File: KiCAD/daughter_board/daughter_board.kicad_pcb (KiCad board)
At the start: 2 copper layers, 41 x 33 mm, 29 parts, among them IC1 QMC5883L, J1 JST, J2 S2B-PH-SM4-TB_LF__SN_2mm, U1 TPS61023DRLR, U2 SN74AHCT1G125DBVR, U3 XIAO-ESP32-C3-SMD, U4 MPU-6050

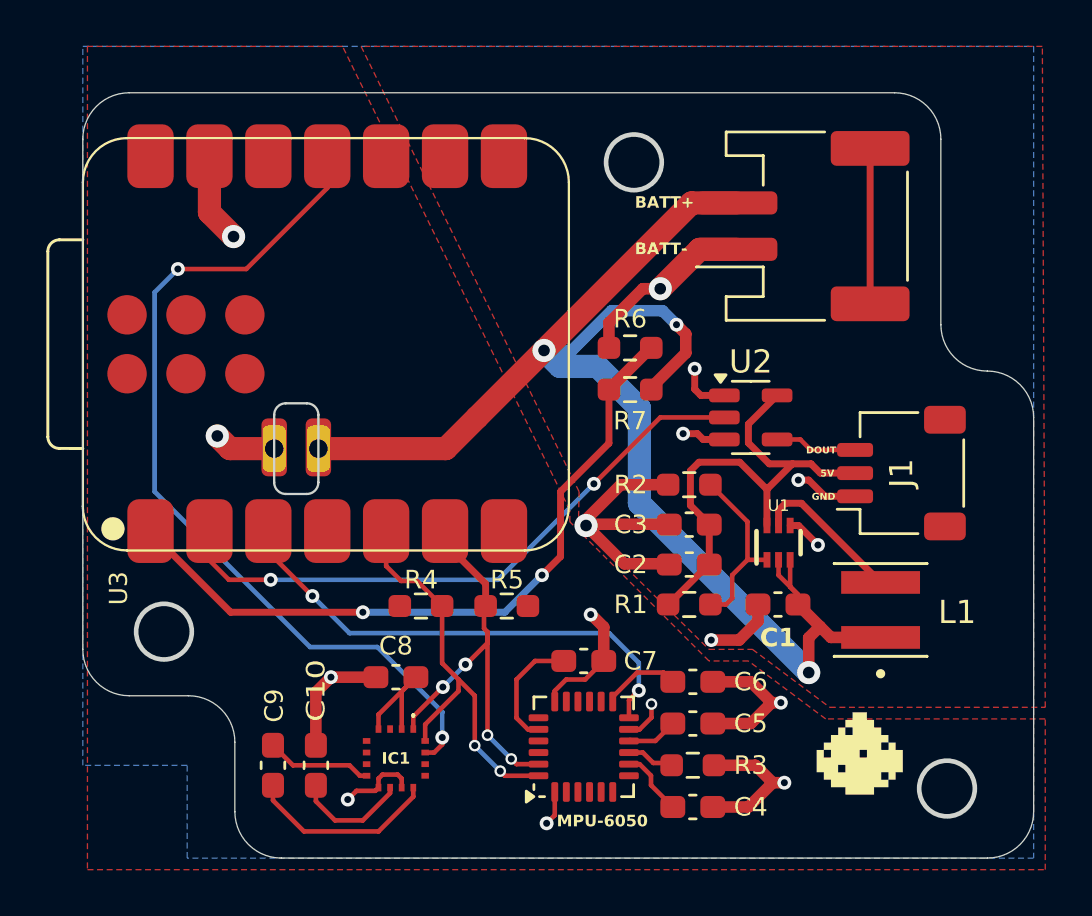
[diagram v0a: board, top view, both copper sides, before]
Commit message: in the pcb of daughter board, change the ground pour plane from top to bottom and power plane from bottom to top
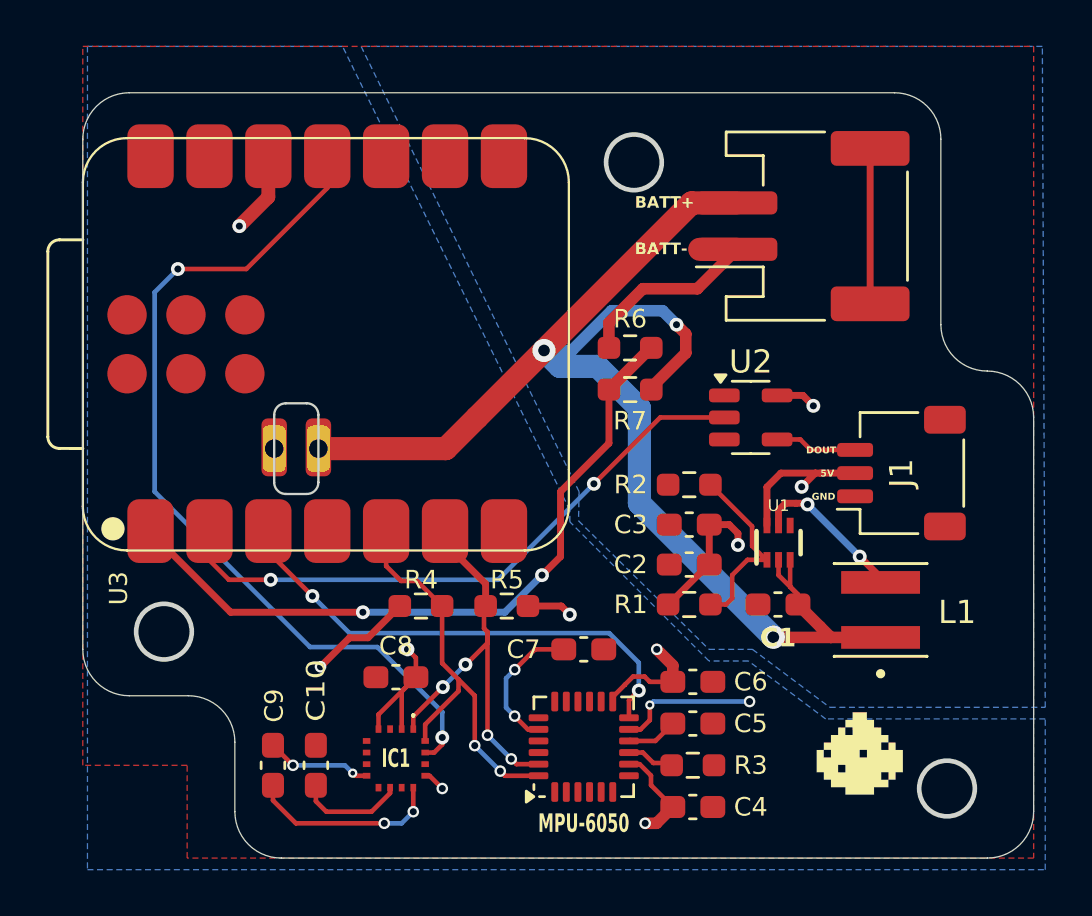
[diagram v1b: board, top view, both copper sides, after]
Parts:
- moved C7 0.50 mm to (104.6, 63.0)
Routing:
- net -BATT: track 68.1 -> 15.6 mm, vias 16 -> 2
- net /3V3: track 11.8 -> 27.3 mm, vias 0 -> 7
- net /5V: track 21.6 -> 14.8 mm, vias 0 -> 3
- net +BATT: track 62.5 -> 60.6 mm
- net Net-(U4-CPOUT): track 5.18 -> 6.05 mm, vias 0 -> 2
- net Net-(U1-SW): track 6.60 -> 6.72 mm, vias 0 -> 2
- net Net-(IC1-SETC): track 8.26 -> 8.35 mm, vias 0 -> 2
- net Net-(IC1-STEP): vias 0 -> 2
- added copper zone on F.Cu, net -BATT
- added copper zone on B.Cu, net /3V3
- added copper zone on B.Cu, net /5V
- removed copper zone on B.Cu, net -BATT
- removed copper zone on F.Cu, net /3V3
- removed copper zone on F.Cu, net /5V

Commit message: changed the min via hole so that min via hole=0.3mm
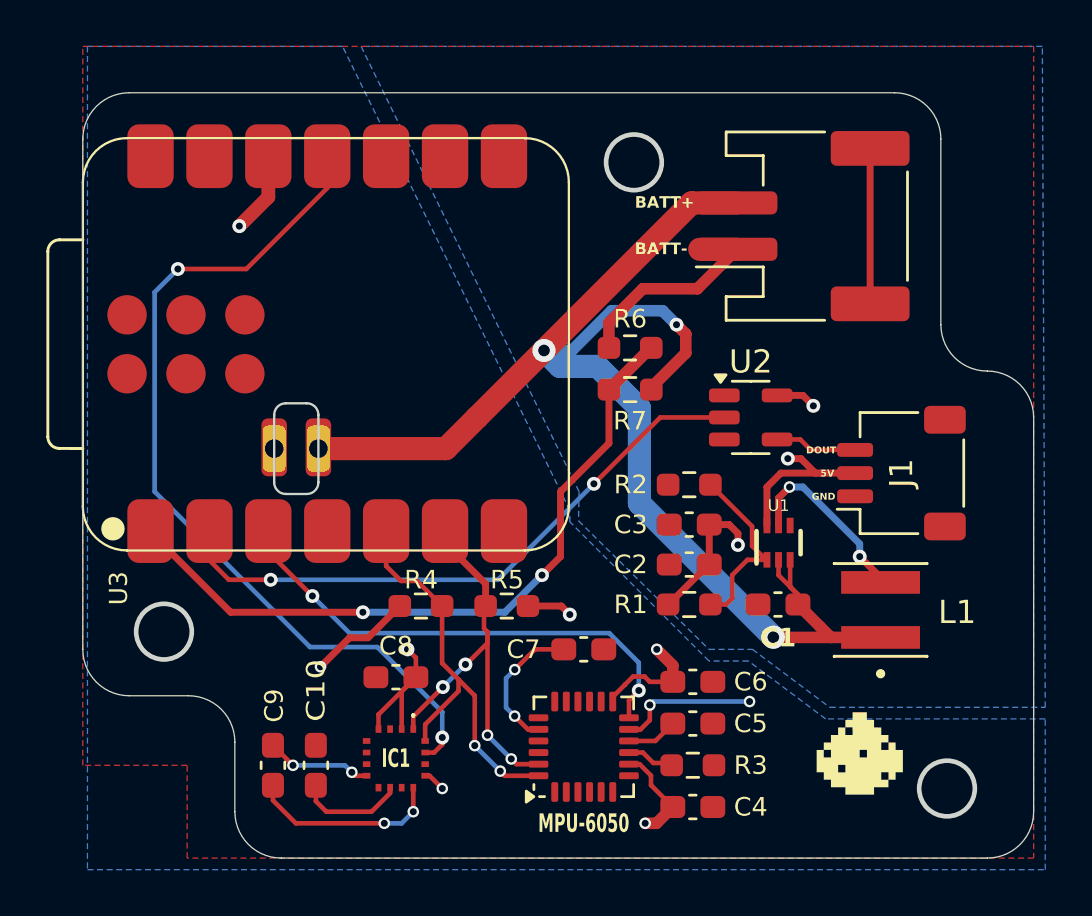
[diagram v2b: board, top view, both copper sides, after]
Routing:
- net Net-(U1-SW): track 6.72 -> 7.93 mm
- net /5V: track 14.8 -> 15.4 mm
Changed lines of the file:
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@@
 	(via
 		(at 107.45 65.4)
-		(size 0.4)
-		(drill 0.2)
+		(size 0.5)
+		(drill 0.3)
 		(layers "F.Cu" "B.Cu")
 		(net 2)
@@
 	)
 	(segment
-		(start 113.997017 55.991051)
-		(end 114.588068 55.4)
-		(width 0.3)
-		(layer "F.Cu")
-		(net 3)
-	)
-	(segment
 		(start 112.498998 57.659999)
 		(end 112.498997 56.001003)
@@
 	)
 	(segment
+		(start 113.4 54.775)
+		(end 113.963068 54.775)
+		(width 0.3)
+		(layer "F.Cu")
+		(net 3)
+	)
+	(segment
 		(start 112.498997 56.001003)
 		(end 113.1 55.4)
@@
 		(net 3)
 	)
+	(segment
+		(start 113.963068 54.775)
+		(end 114.588068 55.4)
+		(width 0.3)
+		(layer "F.Cu")
+		(net 3)
+	)
 	(via
 		(at 111.25 58.5)
@@
 	)
 	(via
-		(at 113.997017 55.991051)
+		(at 113.4 54.775)
 		(size 0.6)
 		(drill 0.3)
@@
 	(segment
 		(start 94.75 68.45)
-		(end 95.237 68.45)
+		(end 94.6 68.3)
 		(width 0.2)
 		(layer "F.Cu")
@@
 	)
 	(segment
-		(start 94.638928 68.338928)
+		(start 95.237 68.45)
 		(end 94.75 68.45)
 		(width 0.2)
@@
 	)
 	(via
-		(at 94.638928 68.338928)
-		(size 0.4)
-		(drill 0.2)
+		(at 94.6 68.3)
+		(size 0.5)
+		(drill 0.3)
 		(layers "F.Cu" "B.Cu")
 		(net 8)
@@
 	)
 	(segment
-		(start 94.638928 68.338928)
+		(start 94.6 68.3)
 		(end 94.3 68)
 		(width 0.2)
@@
 	)
 	(segment
-		(start 113.3 56.7)
-		(end 113.75 56.7)
-		(width 0.3)
-		(layer "F.Cu")
-		(net 20)
-	)
-	(segment
 		(start 117.4 59.9)
 		(end 117.4 60.115)
@@
 	)
 	(segment
-		(start 113.75 56.7)
-		(end 114.2 56.7)
-		(width 0.3)
-		(layer "F.Cu")
-		(net 20)
-	)
-	(segment
-		(start 114.2 56.7)
-		(end 114.25 56.75)
-		(width 0.3)
-		(layer "F.Cu")
-		(net 20)
-	)
-	(segment
 		(start 116.5 59)
 		(end 117.4 59.9)
@@
 	)
 	(segment
-		(start 112.999997 57.000003)
-		(end 113.3 56.7)
+		(start 113 56.475)
+		(end 113.475 56)
 		(width 0.3)
 		(layer "F.Cu")
@@
 	)
 	(segment
+		(start 113 57.659996)
+		(end 113 56.475)
+		(width 0.3)
+		(layer "F.Cu")
+		(net 20)
+	)
+	(segment
 		(start 112.999997 57.659999)
-		(end 112.999997 57.000003)
+		(end 113 57.659996)
 		(width 0.3)
 		(layer "F.Cu")
@@
 	)
 	(via
-		(at 114.25 56.75)
-		(size 0.6)
+		(at 113.475 56)
+		(size 0.5)
 		(drill 0.3)
 		(layers "F.Cu" "B.Cu")
@@
 	)
 	(segment
-		(start 114.25 56.75)
+		(start 116.5 58.45)
 		(end 116.5 59)
 		(width 0.3)
 		(layer "B.Cu")
+		(net 20)
+	)
+	(segment
+		(start 113.475 56)
+		(end 114.05 56)
+		(width 0.3)
+		(layer "B.Cu")
+		(net 20)
+	)
+	(segment
+		(start 114.05 56)
+		(end 116.5 58.45)
+		(width 0.3)
+		(layer "B.Cu")

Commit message: changed the readme images
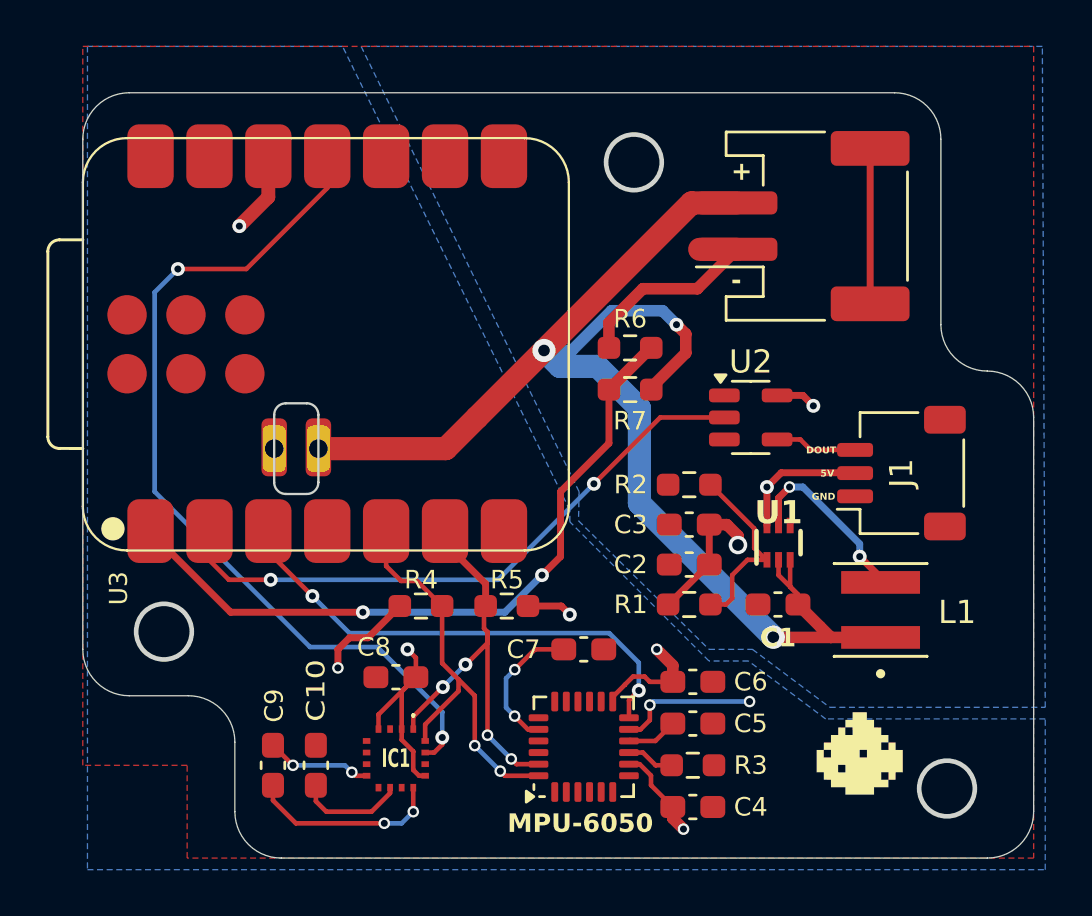
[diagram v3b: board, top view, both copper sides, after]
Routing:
- net /5V: track 15.4 -> 13.5 mm
- net /3V3: track 27.3 -> 28.4 mm, vias 7 -> 6
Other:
- board text added: "DOUT"
- board text added: "GND"

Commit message: due to clearence issue of the power connecter in the daughter baord- changed the 2mm jst to 1mm jst, also updated the 3d model in freecad
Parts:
- removed J2: S2B-PH-SM4-TB_LF__SN_2mm, Connector_JST:JST_PH_S2B-PH-SM4-TB_1x02-1MP_P2.00mm_Horizontal
- added J3: SM02B-SRSS-TB_LF__SN_, Connector_JST:SM02B-SRSS-TB_LF__SN_, F.Cu at (111.8, 45.5)
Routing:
- net Net-(J2-SHIELD): track 6.70 -> 0.00 mm
- net -BATT: track 15.6 -> 18.8 mm
- net +BATT: track 60.6 -> 58.7 mm
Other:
- outline, holes or cut-outs redrawn
- board text added: "+"
- board text added: "-"
- board text added: "v3"

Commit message: touch on the daughter board silkscreen
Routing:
- net +BATT: track 58.7 -> 59.5 mm
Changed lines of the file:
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@@
 		(tags "TPS61023DRLR ")
 		(property "Reference" "U1"
-			(at 1.3 0 0)
+			(at 1.7 0 0)
 			(unlocked yes)
 			(layer "F.SilkS")
 			(effects
 				(font
-					(size 1 1)
+					(size 0.8 0.8)
 					(thickness 0.15)
 					(bold yes)
@@
 		(tags "capacitor handsolder")
 		(property "Reference" "C1"
-			(at -0.000001 -1.435001 0)
+			(at -1.125001 -1.435001 0)
 			(layer "F.SilkS")
 			(effects
@@
 		(at 117.4 61.3 90)
 		(property "Reference" "L1"
-			(at -0.1 3.3 0)
+			(at -3 1.5 0)
 			(layer "F.SilkS")
 			(effects
@@
 	)
 	(segment
-		(start 115.2575 62.485)
-		(end 114.78625 62.01375)
-		(width 0.5)
+		(start 113.837499 60.637499)
+		(end 112.999997 59.799997)
+		(width 0.2)
 		(layer "F.Cu")
 		(net 1)
 	)
 	(segment
-		(start 113.837499 60.637499)
-		(end 112.999997 59.799997)
-		(width 0.2)
+		(start 114.5 62.485)
+		(end 113.837499 61.822499)
+		(width 0.5)
 		(layer "F.Cu")
 		(net 1)
@@
 	)
 	(segment
+		(start 115.6 62.485)
+		(end 115.2575 62.485)
+		(width 0.5)
+		(layer "F.Cu")
+		(net 1)
+	)
+	(segment
 		(start 112.999997 59.799997)
 		(end 112.999997 59.140001)
@@
 	)
 	(segment
+		(start 113.837499 61.822499)
+		(end 113.837499 61.064999)
+		(width 0.5)
+		(layer "F.Cu")
+		(net 1)
+	)
+	(segment
 		(start 113.837499 60.637499)
 		(end 113.499999 60.299999)
@@
 	)
 	(segment
-		(start 114.78625 62.01375)
-		(end 113.837499 61.064999)
-		(width 0.5)
-		(layer "F.Cu")
-		(net 1)
-	)
-	(segment
 		(start 113.837499 61.064999)
 		(end 113.837499 60.637499)
@@
 		(width 0.5)
 		(layer "F.Cu")
+		(net 1)
+	)
+	(segment
+		(start 115.2575 62.485)
+		(end 114.5 62.485)
+		(width 0.5)
+		(layer "F.Cu")

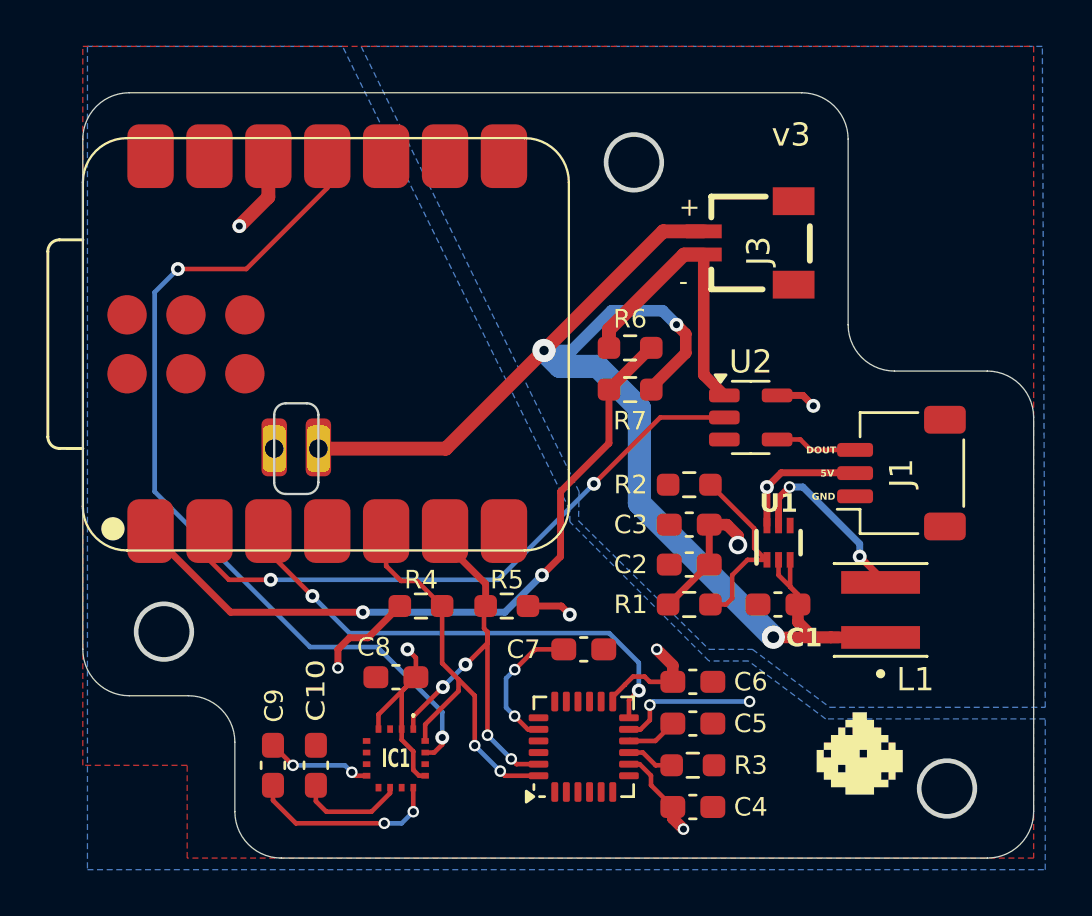
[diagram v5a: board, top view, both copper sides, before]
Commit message: changed the schematic and pads of C and R to non-handsolder ones
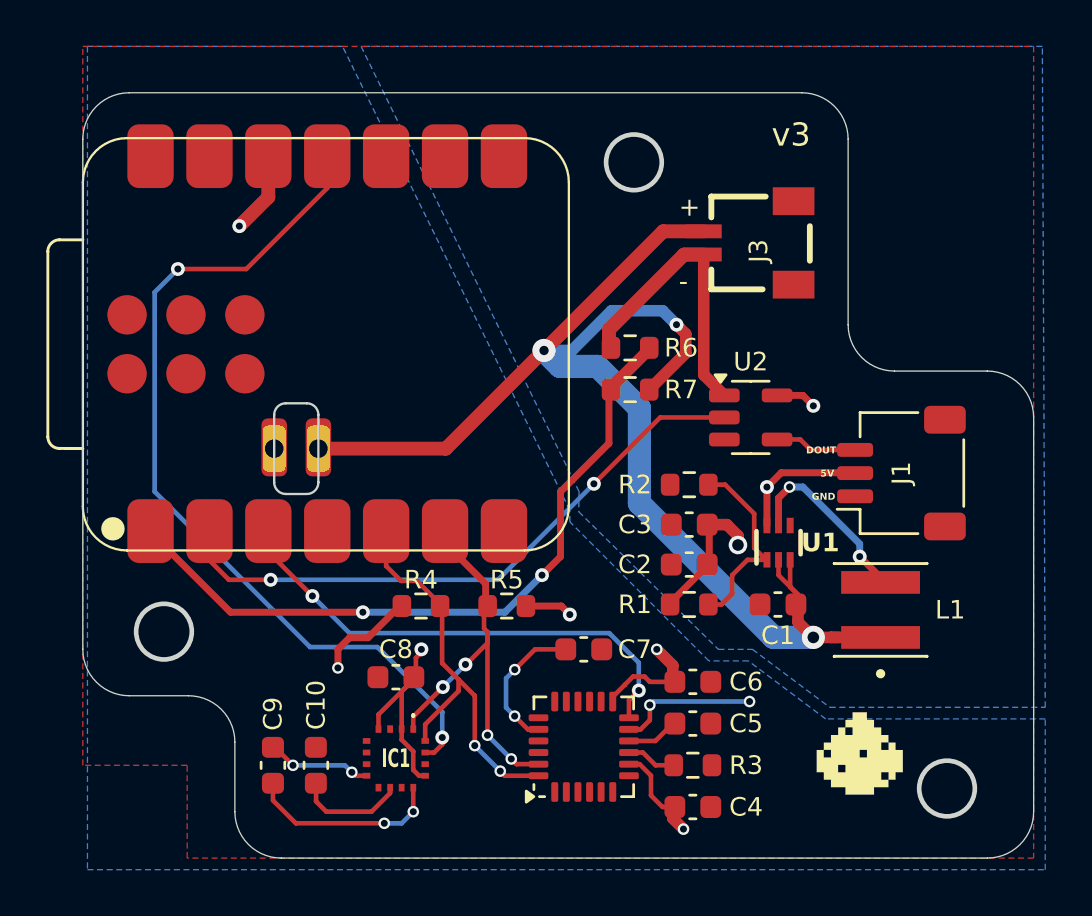
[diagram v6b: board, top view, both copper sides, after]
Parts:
- C1, C10, C2, C3, C4, C5, C6, C7, C8, C9: footprint Capacitor_SMD:C_0603_1608Metric_Pad1.08x0.95mm_HandSolder -> Capacitor_SMD:C_0603_1608Metric
- R1, R2, R3, R4, R5, R6, R7: footprint Resistor_SMD:R_0603_1608Metric_Pad0.98x0.95mm_HandSolder -> Resistor_SMD:R_0603_1608Metric
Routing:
- net +BATT: track 59.5 -> 58.7 mm
